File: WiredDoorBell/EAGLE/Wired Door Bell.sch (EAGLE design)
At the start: 12 parts, among them T1 2N2222

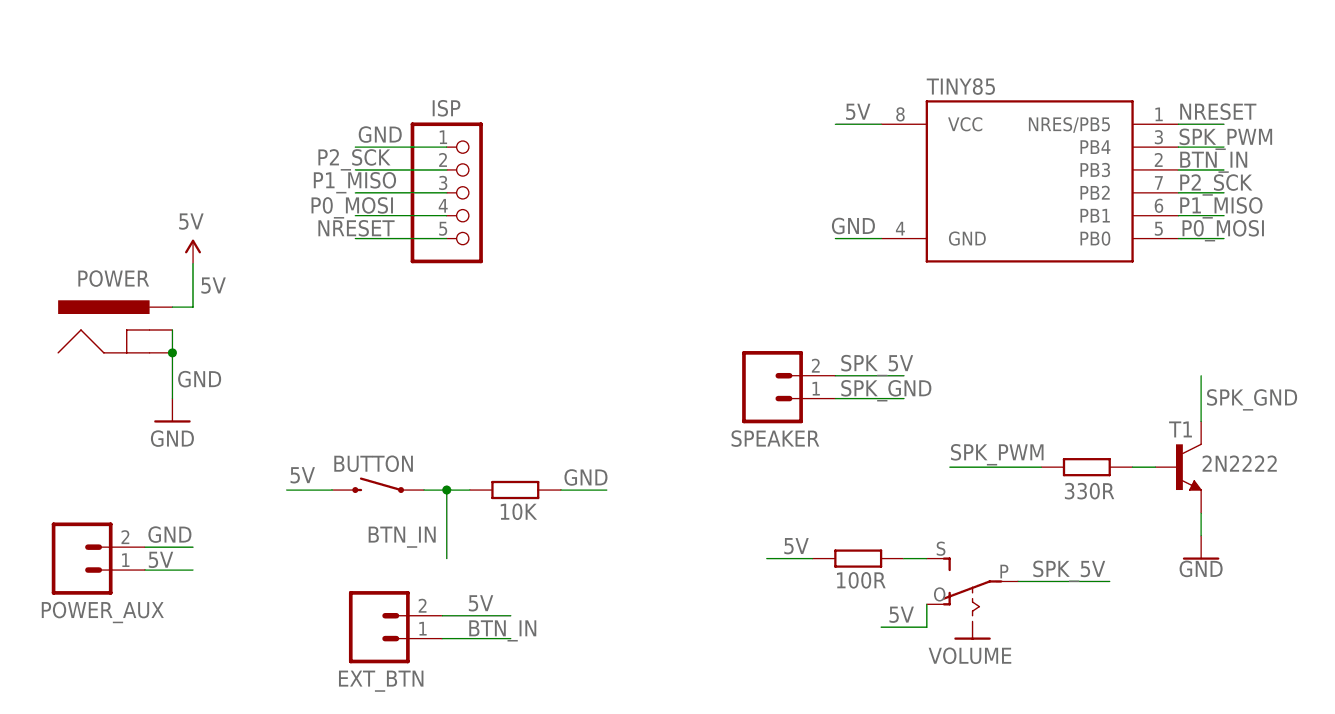
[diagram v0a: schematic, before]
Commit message: Eagle : Fixed Schematics, Board and PCB
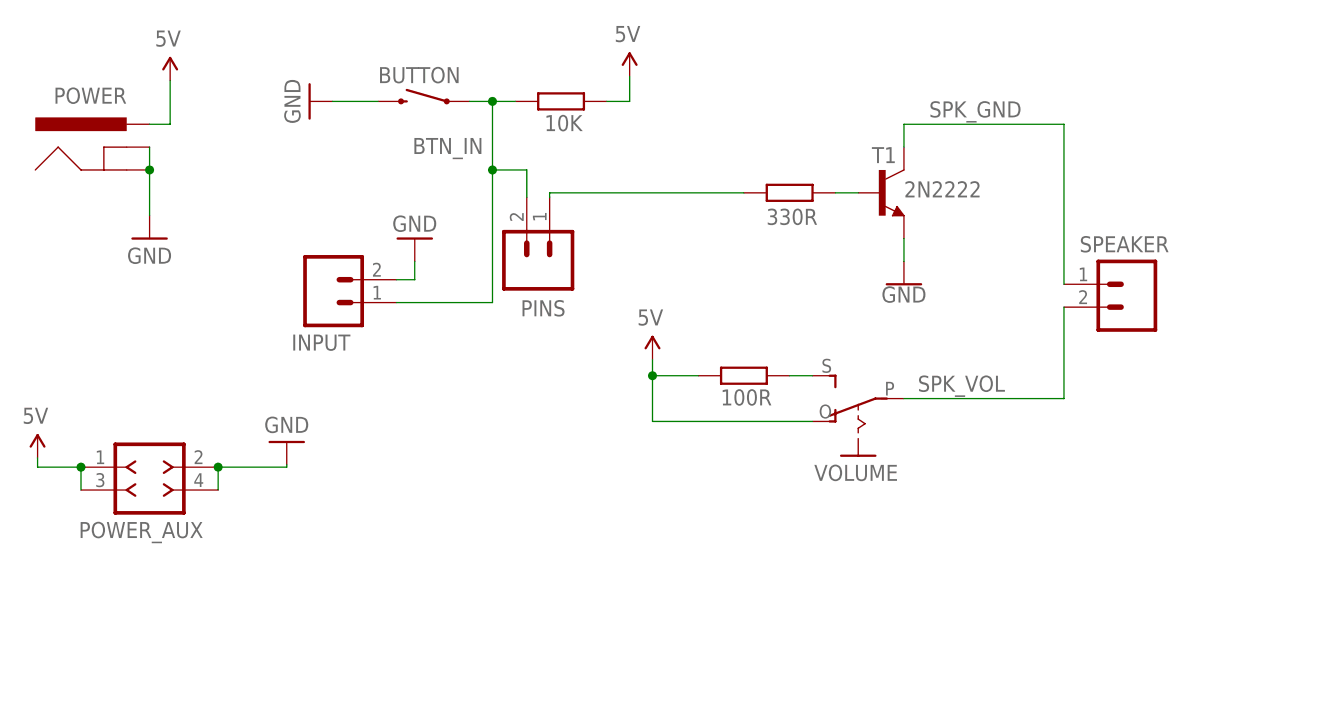
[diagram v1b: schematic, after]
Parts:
- removed EXT_BTN: (no value), SparkFun-Connectors:CONN_02
- removed ISP: (no value), pinhead:PINHD-1X5
- removed TINY85: ATTINY85-20P, _hhn_attiny25_45_85:ATTINY85-20P
- added INPUT, PINS: (no value), SparkFun-Connectors:CONN_02
- POWER_AUX: value (none) -> F-2X02-DIL-100; device SparkFun-Connectors:CONN_02 -> con-headers-jp:F-2X02-DIL-100
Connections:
- net SPK_5V renamed SPK_VOL
- removed net NRESET: ISP.5, TINY85.NRES/PB5
- removed net P0_MOSI: ISP.4, TINY85.PB0
- removed net P1_MISO: ISP.3, TINY85.PB1
- removed net P2_SCK: ISP.2, TINY85.PB2
- net 5V: now also 10K.2, POWER_AUX.3; no longer BUTTON.2, EXT_BTN.2, TINY85.VCC
- net BTN_IN: now also INPUT.1, PINS.2; no longer EXT_BTN.1, TINY85.PB3
- net GND: now also BUTTON.2, INPUT.2, POWER_AUX.4; no longer 10K.2, ISP.1, TINY85.GND
- net SPK_PWM: now also PINS.1; no longer TINY85.PB4
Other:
- moved on the sheet: 100R, 10K, 330R, BUTTON, POWER, SPEAKER, T1, VOLUME
